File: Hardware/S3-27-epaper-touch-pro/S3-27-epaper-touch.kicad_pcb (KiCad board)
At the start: 4 copper layers, 65.4 x 71 mm, 61 parts, among them J1 AFC24-S24FIC-00, J2 USB_C_Programming, J3 Conn_01x06, J4 Conn_01x06_Female, J5 Groove sensor, J6 Conn_01x06, Q1 Si1308, Q2 BC817, Q3 BC817, U1 ESP32-S3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

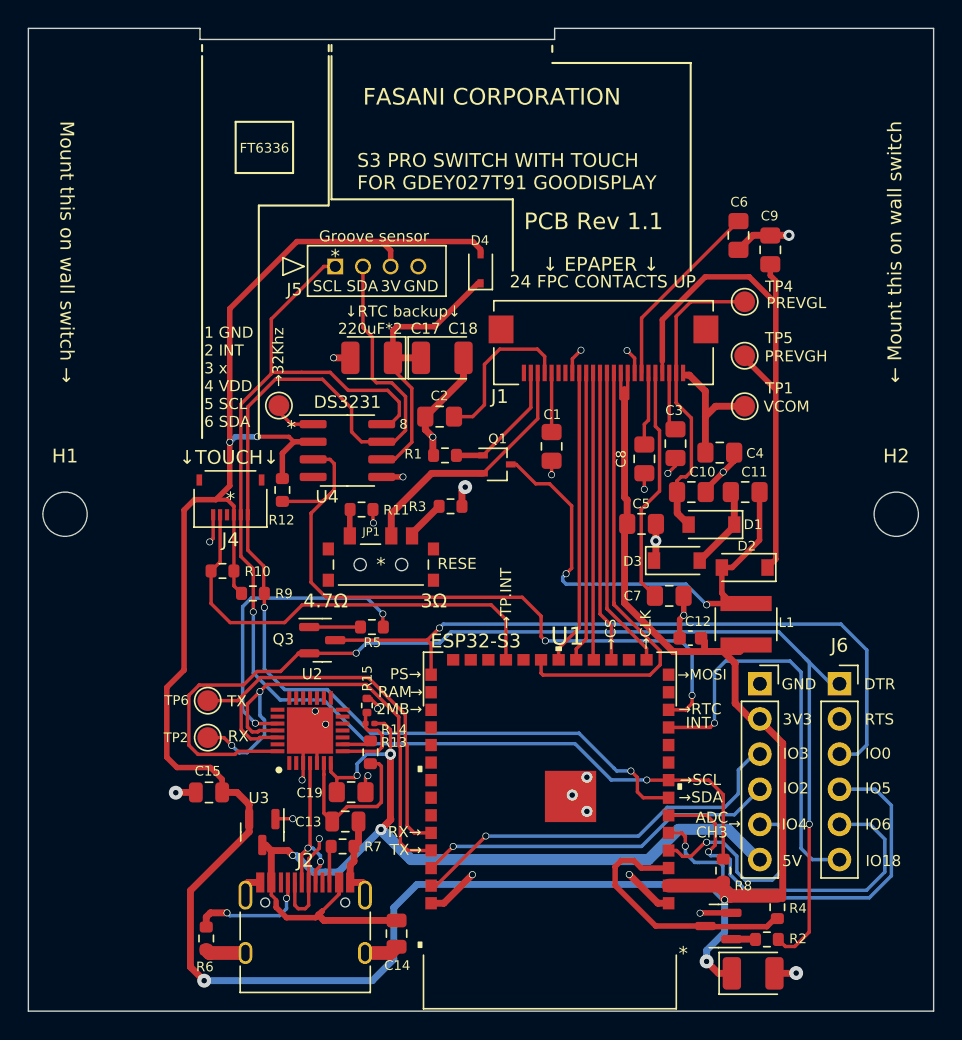
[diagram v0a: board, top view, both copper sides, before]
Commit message: Add files via upload
Changes
R16 0R = IO46 Resistor for Compatibility to ESP32 WROOM
R15 changed package to 0603(was 0402)
Fixed Layout error at R15
Rerouted RTS Line to enable 2 Layer Board
Rerouted 3.3V next to J3
Changed orientation of C3
Routed IO18 to J7 to make space for USB Host
Added USB Port J7

TODO:
Need to double check usage of ESP32 Wroom if they are compatible to current pinning
(NOT with current pinning)
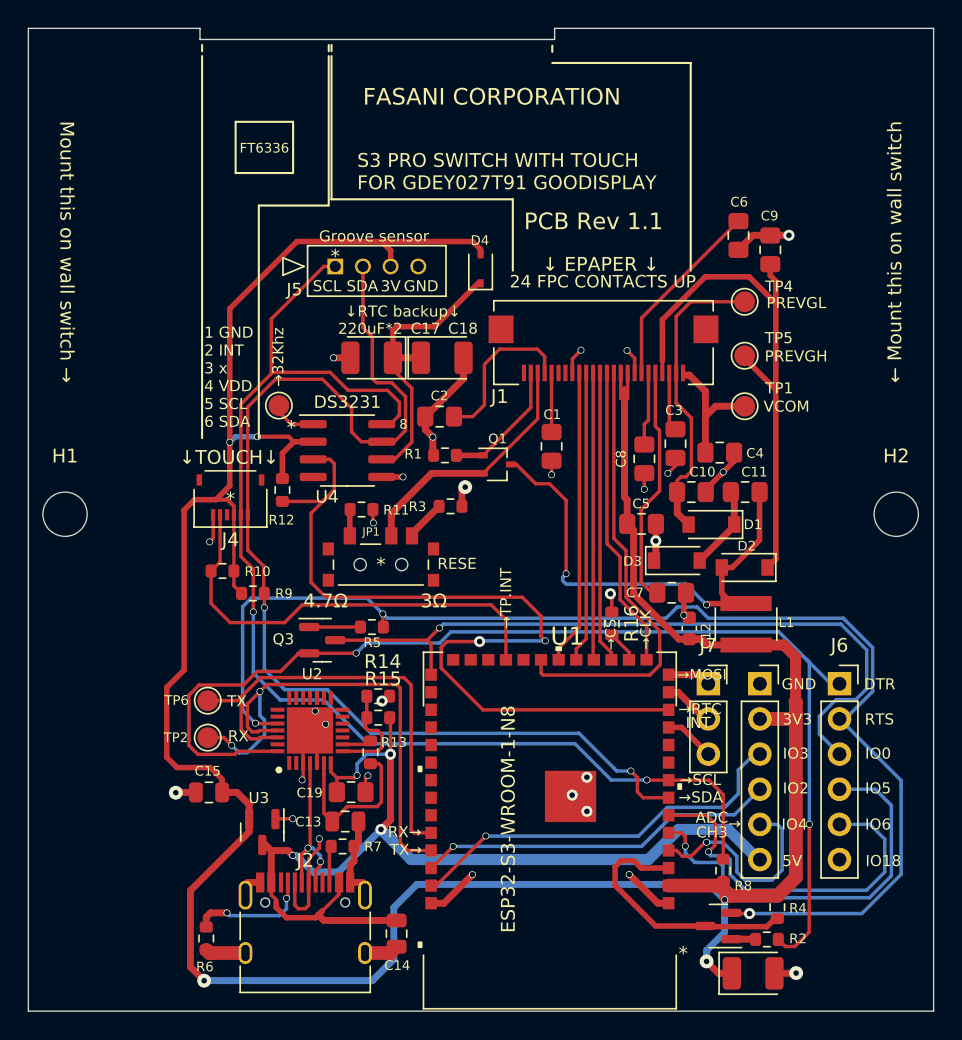
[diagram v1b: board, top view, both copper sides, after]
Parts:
- added J7: Conn_01x03, Connector_PinSocket_2.54mm:PinSocket_1x03_P2.54mm_Vertical, F.Cu at (153.9, 102.3)
- added R16: 0R, Resistor_SMD:R_0603_1608Metric, F.Cu at (146.9, 98.0)
- R14: footprint Resistor_SMD:R_0201_0603Metric -> Resistor_SMD:R_0603_1608Metric
- R15: footprint Resistor_SMD:R_0402_1005Metric -> Resistor_SMD:R_0603_1608Metric
- U1: value ESP32-S3 -> ESP32-S3-WROOM-1-N8
- moved R15 1.06 mm to (130.1, 103.2), turned to 180 degrees
- moved R14 0.73 mm to (130.1, 104.8)
- moved C12 0.70 mm to (152.6, 98.3), turned to -90 degrees
- moved C7 0.29 mm to (151.3, 95.8)
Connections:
- J6 pad 6: /IO_18 -> unconnected-(J6-Pad6)
- U1 pad 13: unconnected-(U1-Pad13) -> /USB_D-
- U1 pad 14: unconnected-(U1-Pad14) -> /USB_D+
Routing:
- net /IO_18: track 29.9 -> 3.67 mm, vias 1 -> 0
- net /3231_INT: track 51.1 -> 61.5 mm
- net /RTS: track 85.9 -> 92.2 mm
- net /USB_D-: track 0.00 -> 3.67 mm
- net /USB_D+: track 0.00 -> 3.14 mm
- net unconnected-(U1-Pad16): track 0.00 -> 2.31 mm
- net +3V3: track 209.9 -> 211.4 mm
- net TX: track 31.4 -> 32.9 mm
- net Net-(R14-Pad1): track 6.40 -> 7.81 mm
- net RX: track 36.5 -> 37.8 mm
- net /IO_0: track 51.4 -> 52.6 mm
- net GND: track 77.8 -> 76.5 mm, vias 29 -> 30
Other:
- board text removed: "2MB→"
- board text removed: "PS→"
- board text removed: "RAM"
